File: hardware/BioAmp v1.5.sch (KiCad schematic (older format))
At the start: 28 parts, among them J1 Conn_01x02_Male, J2 PJ-3062-CO, J4 Conn_01x03_Male, J5 Conn_01x02_Male, J6 Conn_01x02_Male, J7 Conn_01x02_Male, SW1 G64_DPDT_7x7x12mm, U1 TL074

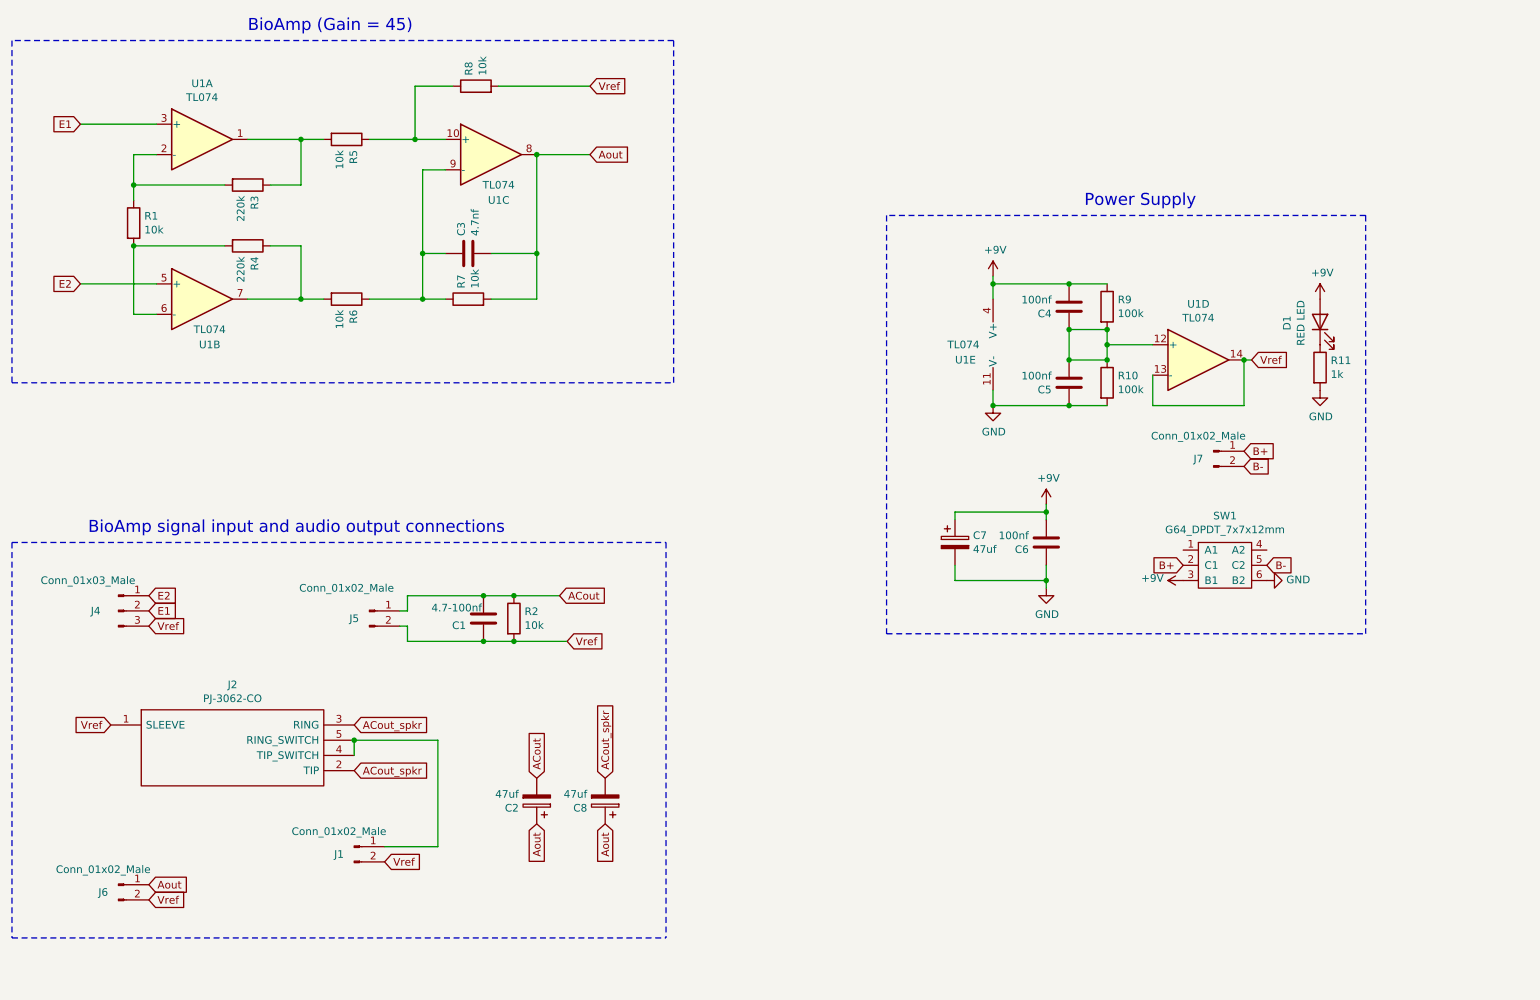
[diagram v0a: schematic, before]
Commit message: BioAmp v1.5.7 hardware files
Small modification for the holes in this update.
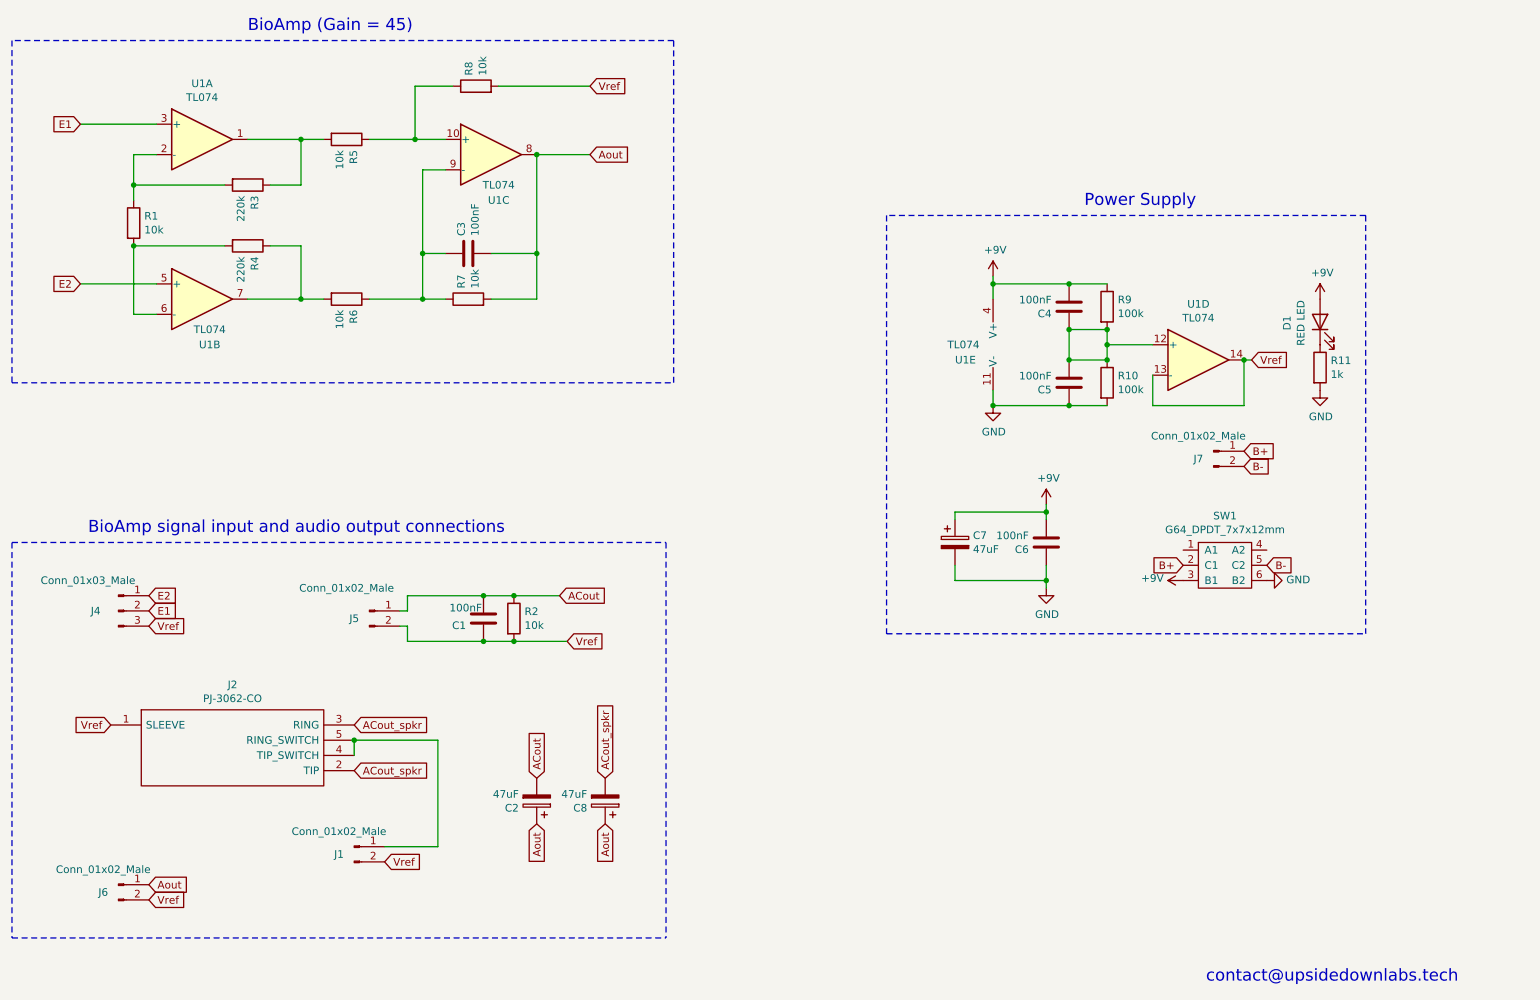
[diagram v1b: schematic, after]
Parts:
- C1: value 4.7-100nf -> 100nF
- C2, C7, C8: value 47uf -> 47uF
- C3: value 4.7nf -> 100nF
- C4, C5, C6: value 100nf -> 100nF
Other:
- note added: "contact@upsidedownlabs.tech"
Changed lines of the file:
@@
 Sheet 1 1
 Title "BioAmp v1.5"
-Date "2021-07-07"
-Rev "v1.5.6"
+Date "2021-07-29"
+Rev "v1.5.7"
 Comp "Upside Down Labs"
 Comment1 "Compatible with BYB Spike Recorder"
@@
 P 8200 3350
 F 0 "C5" H 8315 3396 50  0000 L CNN
-F 1 "100nf" H 8315 3305 50  0000 L CNN
+F 1 "100nF" H 8315 3305 50  0000 L CNN
 F 2 "Capacitor_THT:C_Disc_D3.8mm_W2.6mm_P2.50mm" H 8238 3200 50  0001 C CNN
 F 3 "~" H 8200 3350 50  0001 C CNN
@@
 P 8200 2850
 F 0 "C4" H 8315 2896 50  0000 L CNN
-F 1 "100nf" H 8315 2805 50  0000 L CNN
+F 1 "100nF" H 8315 2805 50  0000 L CNN
 F 2 "Capacitor_THT:C_Disc_D3.8mm_W2.6mm_P2.50mm" H 8238 2700 50  0001 C CNN
 F 3 "~" H 8200 2850 50  0001 C CNN
@@
 P 4250 2500
 F 0 "C3" H 4365 2546 50  0000 L CNN
-F 1 "4.7nf" H 4365 2455 50  0000 L CNN
+F 1 "100nF" H 4365 2455 50  0000 L CNN
 F 2 "Capacitor_THT:C_Disc_D3.8mm_W2.6mm_P2.50mm" H 4288 2350 50  0001 C CNN
 F 3 "~" H 4250 2500 50  0001 C CNN
@@
 P 8050 4400
 F 0 "C6" H 8165 4446 50  0000 L CNN
-F 1 "100nf" H 8165 4355 50  0000 L CNN
+F 1 "100nF" H 8165 4355 50  0000 L CNN
 F 2 "Capacitor_THT:C_Disc_D3.8mm_W2.6mm_P2.50mm" H 8088 4250 50  0001 C CNN
 F 3 "~" H 8050 4400 50  0001 C CNN
@@
 P 7450 4400
 F 0 "C7" H 7568 4446 50  0000 L CNN
-F 1 "47uf" H 7568 4355 50  0000 L CNN
+F 1 "47uF" H 7568 4355 50  0000 L CNN
 F 2 "Capacitor_THT:CP_Radial_D5.0mm_P2.50mm" H 7488 4250 50  0001 C CNN
 F 3 "~" H 7450 4400 50  0001 C CNN
@@
 P 5150 6100
 F 0 "C8" H 5268 6146 50  0000 L CNN
-F 1 "47uf" H 5268 6055 50  0000 L CNN
+F 1 "47uF" H 5268 6055 50  0000 L CNN
 F 2 "Capacitor_THT:CP_Radial_D5.0mm_P2.50mm" H 5188 5950 50  0001 C CNN
 F 3 "~" H 5150 6100 50  0001 C CNN
@@
 P 4700 6100
 F 0 "C2" H 4818 6146 50  0000 L CNN
-F 1 "47uf" H 4818 6055 50  0000 L CNN
+F 1 "47uF" H 4818 6055 50  0000 L CNN
 F 2 "Capacitor_THT:CP_Radial_D5.0mm_P2.50mm" H 4738 5950 50  0001 C CNN
 F 3 "~" H 4700 6100 50  0001 C CNN
@@
 P 4350 4900
 F 0 "C1" H 4465 4946 50  0000 L CNN
-F 1 "4.7-100nf" H 4360 4830 50  0000 L CNN
+F 1 "100nF" H 4360 4830 50  0000 L CNN
 F 2 "Capacitor_THT:C_Disc_D3.8mm_W2.6mm_P2.50mm" H 4388 4750 50  0001 C CNN
 F 3 "~" H 4350 4900 50  0001 C CNN
@@
 EndData
 $EndBitmap
+Text Notes 9100 7300 0    79   ~ 0
+contact@upsidedownlabs.tech
 $EndSCHEMATC
